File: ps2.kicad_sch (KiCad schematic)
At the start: 5 parts, among them J50 Mini-DIN-6, Q10 2N7002

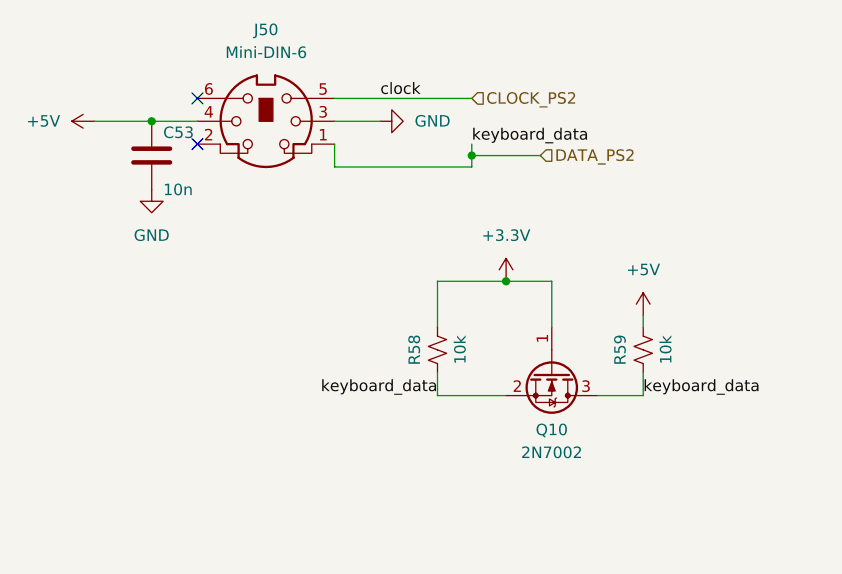
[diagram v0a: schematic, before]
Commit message: se agrego osciloscoio
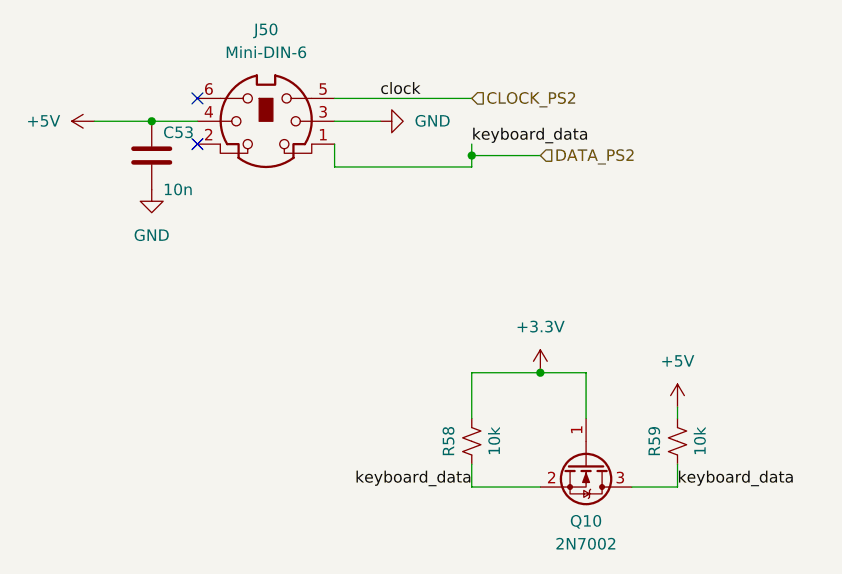
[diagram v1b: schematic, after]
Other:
- moved on the sheet: Q10, R58, R59
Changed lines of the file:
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@@
 	)
 	(junction
-		(at 173.99 111.76)
+		(at 177.8 121.92)
 		(diameter 0)
 		(color 0 0 0 0)
@@
 	(wire
 		(pts
-			(xy 179.07 111.76) (xy 179.07 116.84)
+			(xy 182.88 121.92) (xy 182.88 127)
 		)
 		(stroke
@@
 	(wire
 		(pts
-			(xy 166.37 111.76) (xy 173.99 111.76)
-		)
-		(stroke
-			(width 0)
-			(type default)
-		)
-	)
-	(wire
-		(pts
-			(xy 166.37 124.46) (xy 173.99 124.46)
-		)
-		(stroke
-			(width 0)
-			(type default)
-		)
-	)
-	(wire
-		(pts
-			(xy 166.37 121.92) (xy 166.37 124.46)
-		)
-		(stroke
-			(width 0)
-			(type default)
-		)
-	)
-	(wire
-		(pts
-			(xy 189.23 121.92) (xy 189.23 124.46)
+			(xy 170.18 121.92) (xy 177.8 121.92)
+		)
+		(stroke
+			(width 0)
+			(type default)
+		)
+	)
+	(wire
+		(pts
+			(xy 170.18 134.62) (xy 177.8 134.62)
+		)
+		(stroke
+			(width 0)
+			(type default)
+		)
+	)
+	(wire
+		(pts
+			(xy 170.18 132.08) (xy 170.18 134.62)
+		)
+		(stroke
+			(width 0)
+			(type default)
+		)
+	)
+	(wire
+		(pts
+			(xy 193.04 132.08) (xy 193.04 134.62)
 		)
 		(stroke
@@
 	(wire
 		(pts
-			(xy 184.15 124.46) (xy 189.23 124.46)
+			(xy 187.96 134.62) (xy 193.04 134.62)
 		)
 		(stroke
@@
 	(wire
 		(pts
-			(xy 189.23 115.57) (xy 189.23 116.84)
-		)
-		(stroke
-			(width 0)
-			(type default)
-		)
-	)
-	(wire
-		(pts
-			(xy 173.99 111.76) (xy 179.07 111.76)
-		)
-		(stroke
-			(width 0)
-			(type default)
-		)
-	)
-	(wire
-		(pts
-			(xy 166.37 111.76) (xy 166.37 116.84)
+			(xy 193.04 125.73) (xy 193.04 127)
+		)
+		(stroke
+			(width 0)
+			(type default)
+		)
+	)
+	(wire
+		(pts
+			(xy 177.8 121.92) (xy 182.88 121.92)
+		)
+		(stroke
+			(width 0)
+			(type default)
+		)
+	)
+	(wire
+		(pts
+			(xy 170.18 121.92) (xy 170.18 127)
 		)
 		(stroke
@@
 	)
 	(label "keyboard_data"
-		(at 166.37 124.46 180)
+		(at 170.18 134.62 180)
 		(effects
 			(font
@@
 	)
 	(label "keyboard_data"
-		(at 189.23 124.46 0)
+		(at 193.04 134.62 0)
 		(effects
 			(font
@@
 	(symbol
 		(lib_id "Transistor_FET:2N7002")
-		(at 179.07 121.92 270)
+		(at 182.88 132.08 270)
 		(unit 1)
 		(body_style 1)
@@
 		(fields_autoplaced yes)
 		(property "Reference" "Q10"
-			(at 179.07 128.27 90)
+			(at 182.88 138.43 90)
 			(show_name no)
 			(do_not_autoplace no)
@@
 		)
 		(property "Value" "2N7002"
-			(at 179.07 130.81 90)
+			(at 182.88 140.97 90)
 			(show_name no)
 			(do_not_autoplace no)
@@
 		)
 		(property "Footprint" "Package_TO_SOT_SMD:SOT-23"
-			(at 177.165 127 0)
+			(at 180.975 137.16 0)
 			(hide yes)
 			(show_name no)
@@
 		)
 		(property "Datasheet" "https://www.onsemi.com/pub/Collateral/NDS7002A-D.PDF"
-			(at 175.26 127 0)
+			(at 179.07 137.16 0)
 			(hide yes)
 			(show_name no)
@@
 		)
 		(property "Description" "0.115A Id, 60V Vds, N-Channel MOSFET, SOT-23"
-			(at 179.07 121.92 0)
+			(at 182.88 132.08 0)
 			(hide yes)
 			(show_name no)
@@
 	(symbol
 		(lib_id "Device:R_Small_US")
-		(at 166.37 119.38 180)
+		(at 170.18 129.54 180)
 		(unit 1)
 		(body_style 1)
@@
 		(dnp no)
 		(property "Reference" "R58"
-			(at 163.83 119.38 90)
+			(at 167.64 129.54 90)
 			(show_name no)
 			(do_not_autoplace no)
@@
 		)
 		(property "Value" "10k"
-			(at 168.91 119.38 90)
+			(at 172.72 129.54 90)
 			(show_name no)
 			(do_not_autoplace no)
@@
 		)
 		(property "Footprint" "Resistor_SMD:R_0805_2012Metric"
-			(at 166.37 119.38 0)
+			(at 170.18 129.54 0)
 			(hide yes)
 			(show_name no)
@@
 		)
 		(property "Datasheet" ""
-			(at 166.37 119.38 0)
+			(at 170.18 129.54 0)
 			(hide yes)
 			(show_name no)
@@
 		)
 		(property "Description" ""
-			(at 166.37 119.38 0)
+			(at 170.18 129.54 0)
 			(show_name no)
 			(do_not_autoplace no)
@@
 	(symbol
 		(lib_id "power:+5V")
-		(at 189.23 115.57 0)
+		(at 193.04 125.73 0)
 		(unit 1)
 		(body_style 1)
@@
 		(fields_autoplaced yes)
 		(property "Reference" "#PWR0124"
-			(at 189.23 119.38 0)
+			(at 193.04 129.54 0)
 			(hide yes)
 			(show_name no)
@@
 		)
 		(property "Value" "+5V"
-			(at 189.23 110.49 0)
+			(at 193.04 120.65 0)
 			(show_name no)
 			(do_not_autoplace no)
@@
 		)
 		(property "Footprint" ""
-			(at 189.23 115.57 0)
+			(at 193.04 125.73 0)
 			(hide yes)
 			(show_name no)
@@
 		)
 		(property "Datasheet" ""
-			(at 189.23 115.57 0)
+			(at 193.04 125.73 0)
 			(hide yes)
 			(show_name no)
@@
 		)
 		(property "Description" ""
-			(at 189.23 115.57 0)
+			(at 193.04 125.73 0)
 			(show_name no)
 			(do_not_autoplace no)
@@
 	(symbol
 		(lib_id "power:+3.3VA")
-		(at 173.99 111.76 0)
+		(at 177.8 121.92 0)
 		(unit 1)
 		(body_style 1)
@@
 		(fields_autoplaced yes)
 		(property "Reference" "#PWR0125"
-			(at 173.99 115.57 0)
+			(at 177.8 125.73 0)
 			(hide yes)
 			(show_name no)
@@
 		)
 		(property "Value" "+3.3V"
-			(at 173.99 106.68 0)
+			(at 177.8 116.84 0)
 			(show_name no)
 			(do_not_autoplace no)
@@
 		)
 		(property "Footprint" ""
-			(at 173.99 111.76 0)
+			(at 177.8 121.92 0)
 			(hide yes)
 			(show_name no)
@@
 		)
 		(property "Datasheet" ""
-			(at 173.99 111.76 0)
+			(at 177.8 121.92 0)
 			(hide yes)
 			(show_name no)
@@
 		)
 		(property "Description" ""
-			(at 173.99 111.76 0)
+			(at 177.8 121.92 0)
 			(show_name no)
 			(do_not_autoplace no)
@@
 	(symbol
 		(lib_id "Device:R_Small_US")
-		(at 189.23 119.38 180)
+		(at 193.04 129.54 180)
 		(unit 1)
 		(body_style 1)
@@
 		(dnp no)
 		(property "Reference" "R59"
-			(at 186.69 119.38 90)
+			(at 190.5 129.54 90)
 			(show_name no)
 			(do_not_autoplace no)
@@
 		)
 		(property "Value" "10k"
-			(at 191.77 119.38 90)
+			(at 195.58 129.54 90)
 			(show_name no)
 			(do_not_autoplace no)
@@
 		)
 		(property "Footprint" "Resistor_SMD:R_0805_2012Metric"
-			(at 189.23 119.38 0)
+			(at 193.04 129.54 0)
 			(hide yes)
 			(show_name no)
@@
 		)
 		(property "Datasheet" ""
-			(at 189.23 119.38 0)
+			(at 193.04 129.54 0)
 			(hide yes)
 			(show_name no)
@@
 		)
 		(property "Description" ""
-			(at 189.23 119.38 0)
-			(show_name no)
-			(do_not_autoplace no)
+			(at 193.04 129.54 0)
+			(show_name no)
+			(do_not_autoplace no)
